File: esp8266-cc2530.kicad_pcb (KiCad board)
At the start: 2 copper layers, 119.9 x 53.1 mm, 35 parts, among them J1 CC2530_programmingHeader, J2 Conn_Coaxial, U1 WeMos_D1_mini, U2 AMS1117-3.3, U3 CC2530Fxxx, U4 RFX2401C, Y1 32.768kHz, Y2 32MHz

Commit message: progress on layout
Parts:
- removed C17: DNP, Capacitor_SMD:C_0805_2012Metric
- C1, C2, R1, U2: moved to B.Cu
- J1: footprint Connector_PinHeader_2.54mm:PinHeader_2x05_P2.54mm_Vertical_SMD -> Connector_PinHeader_1.27mm:PinHeader_2x05_P1.27mm_Vertical_SMD
- R5: moved to F.Cu
- moved C1 110.9 mm to (147.4, 136.8)
- moved C2 109.9 mm to (147.7, 139.6)
- moved U2 107.4 mm to (148.2, 145.1), turned to 0 degrees
- moved R1 97.3 mm to (139.7, 145.3), turned to 180 degrees
- moved C8 91.2 mm to (165.8, 125.2), turned to 270 degrees
- moved U1 90.0 mm to (118.1, 124.3)
- moved C3 89.4 mm to (151.1, 126.0)
- moved C12 88.7 mm to (158.8, 125.8), turned to 270 degrees
- moved R3 88.2 mm to (172.2, 128.4), turned to 90 degrees
- moved C10 87.6 mm to (157.3, 141.8)
- moved Y1 87.5 mm to (156.2, 138.8)
- moved C15 87.5 mm to (164.4, 129.8)
- moved C13 87.5 mm to (161.7, 132.6)
- moved C14 87.5 mm to (161.7, 130.7)
- moved C16 87.5 mm to (167.1, 132.7)
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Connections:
- R5 pad 1: Net-(J2-Pad1) -> VCC
- R5 pad 2: Net-(C17-Pad2) -> Net-(J1-Pad9)
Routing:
- net VCC: track 0.00 -> 66.7 mm, vias 0 -> 1
- net GND: track 0.00 -> 66.0 mm, vias 0 -> 18
- net /P2_1: track 0.00 -> 43.2 mm, vias 0 -> 1
- net /P1_1: track 0.00 -> 39.9 mm
- net /P2_2: track 0.00 -> 32.0 mm, vias 0 -> 1
- net /P1_0: track 0.00 -> 28.6 mm
- net /ESP_TX: track 0.00 -> 27.5 mm, vias 0 -> 1
- net /ESP_RX: track 0.00 -> 26.2 mm, vias 0 -> 1
- net Net-(R1-Pad2): track 0.00 -> 21.9 mm
- net Net-(J1-Pad9): track 0.00 -> 9.86 mm
- net Net-(C6-Pad2): track 0.00 -> 9.53 mm
- net Net-(C8-Pad2): track 0.00 -> 9.49 mm
- net Net-(C9-Pad2): track 0.00 -> 7.77 mm
- net Net-(R4-Pad1): track 0.00 -> 7.62 mm
- net Net-(C10-Pad2): track 0.00 -> 6.50 mm
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- added copper zone on F.Cu, net GND
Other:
- board size 119.9 x 53.1 mm -> 126.8 x 87.2 mm

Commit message: board laid out
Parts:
- moved L2 1.10 mm to (168.1, 130.8)
- moved C14 1.10 mm to (162.8, 130.7)
- moved C15 1.10 mm to (165.5, 129.8)
- moved C6 0.80 mm to (162.6, 123.2)
- moved C8 0.80 mm to (165.8, 126.0)
- moved Y2 0.80 mm to (162.7, 126.0)
- moved C5 0.38 mm to (151.6, 136.3)
- moved C4 0.20 mm to (150.6, 133.3)
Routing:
- net /~RST: track 0.00 -> 86.2 mm, vias 0 -> 3
- net VCC: track 66.7 -> 135.9 mm, vias 1 -> 9
- net /ESP_TX: track 27.5 -> 22.6 mm
- net /ESP_RX: track 26.2 -> 21.7 mm
- net /P1_0: track 28.6 -> 27.4 mm
- net Net-(C14-Pad1): track 2.42 -> 3.52 mm
- net Net-(C6-Pad2): track 9.53 -> 8.76 mm
- net GND: track 66.0 -> 66.5 mm, vias 18 -> 31
- net (no net): vias 0 -> 2
- added copper zone on B.Cu, net GND

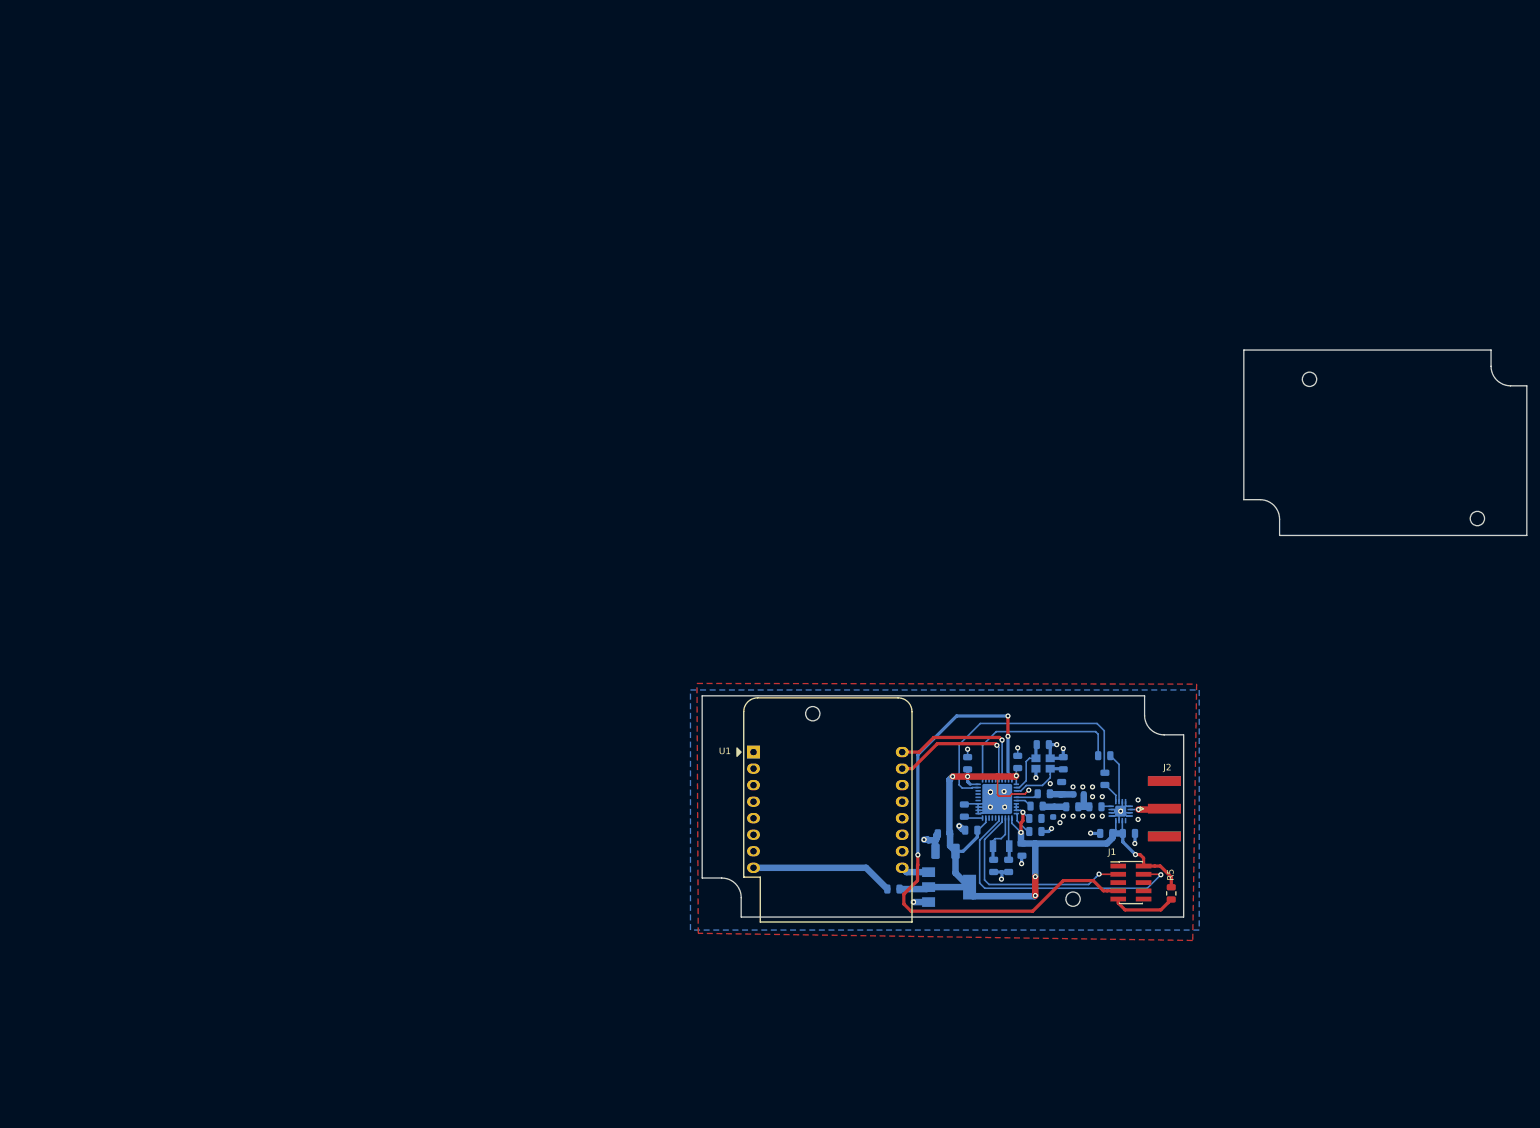
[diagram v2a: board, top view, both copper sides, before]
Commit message: fixed SMA connector footprint and added 3d model.
thinking of changing cases... extra board outlines on edge.cuts
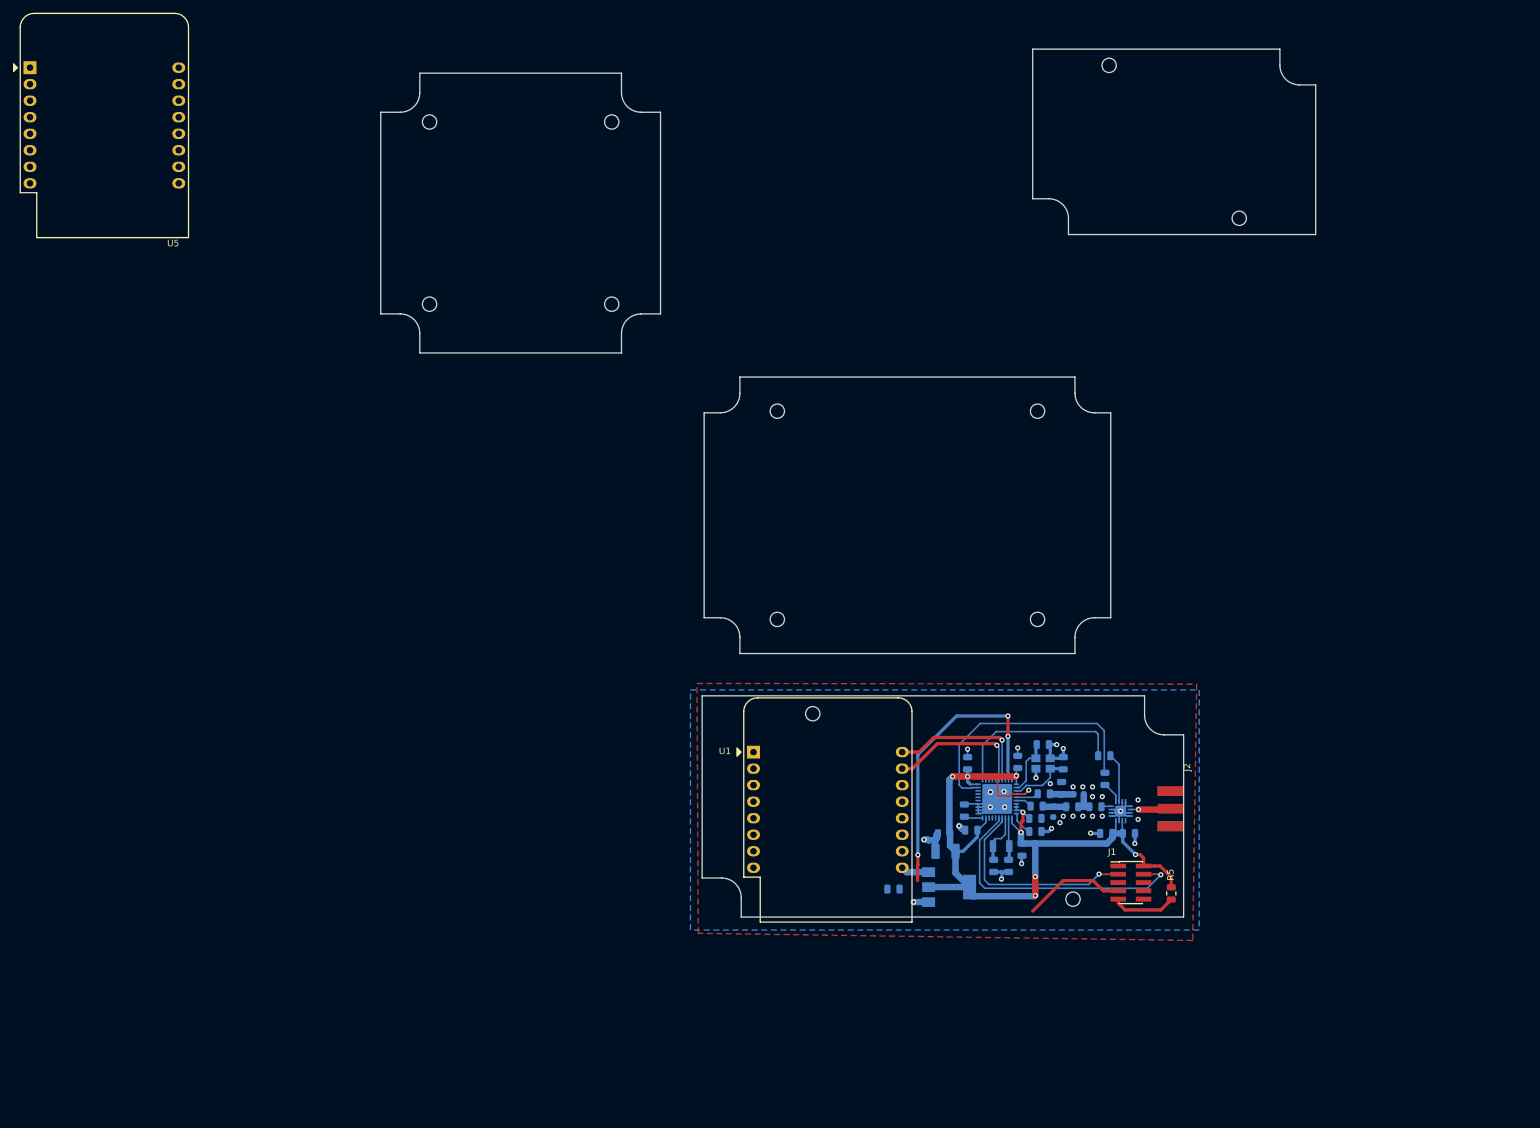
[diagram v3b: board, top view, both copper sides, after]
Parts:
- added U5: WeMos_D1_mini, Module:WEMOS_D1_mini_light, F.Cu at (6.94, 19.1)
- J2: footprint Connector_Coaxial:SMA_Amphenol_132289_EdgeMount -> esp8266-cc2530:CON-SMA-EDGE-S(RP)
- moved J2 0.95 mm to (182.2, 133.0), turned to 270 degrees
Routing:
- net /~RST: track 86.2 -> 61.5 mm
- net Net-(R1-Pad2): track 21.9 -> 0.00 mm
- net VCC: track 135.9 -> 131.7 mm
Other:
- board size 126.8 x 87.2 mm -> 143.7 x 133.4 mm

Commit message: updated layout * new WEMOS D1 footprint and 3d model * switched to case TW5-2-5
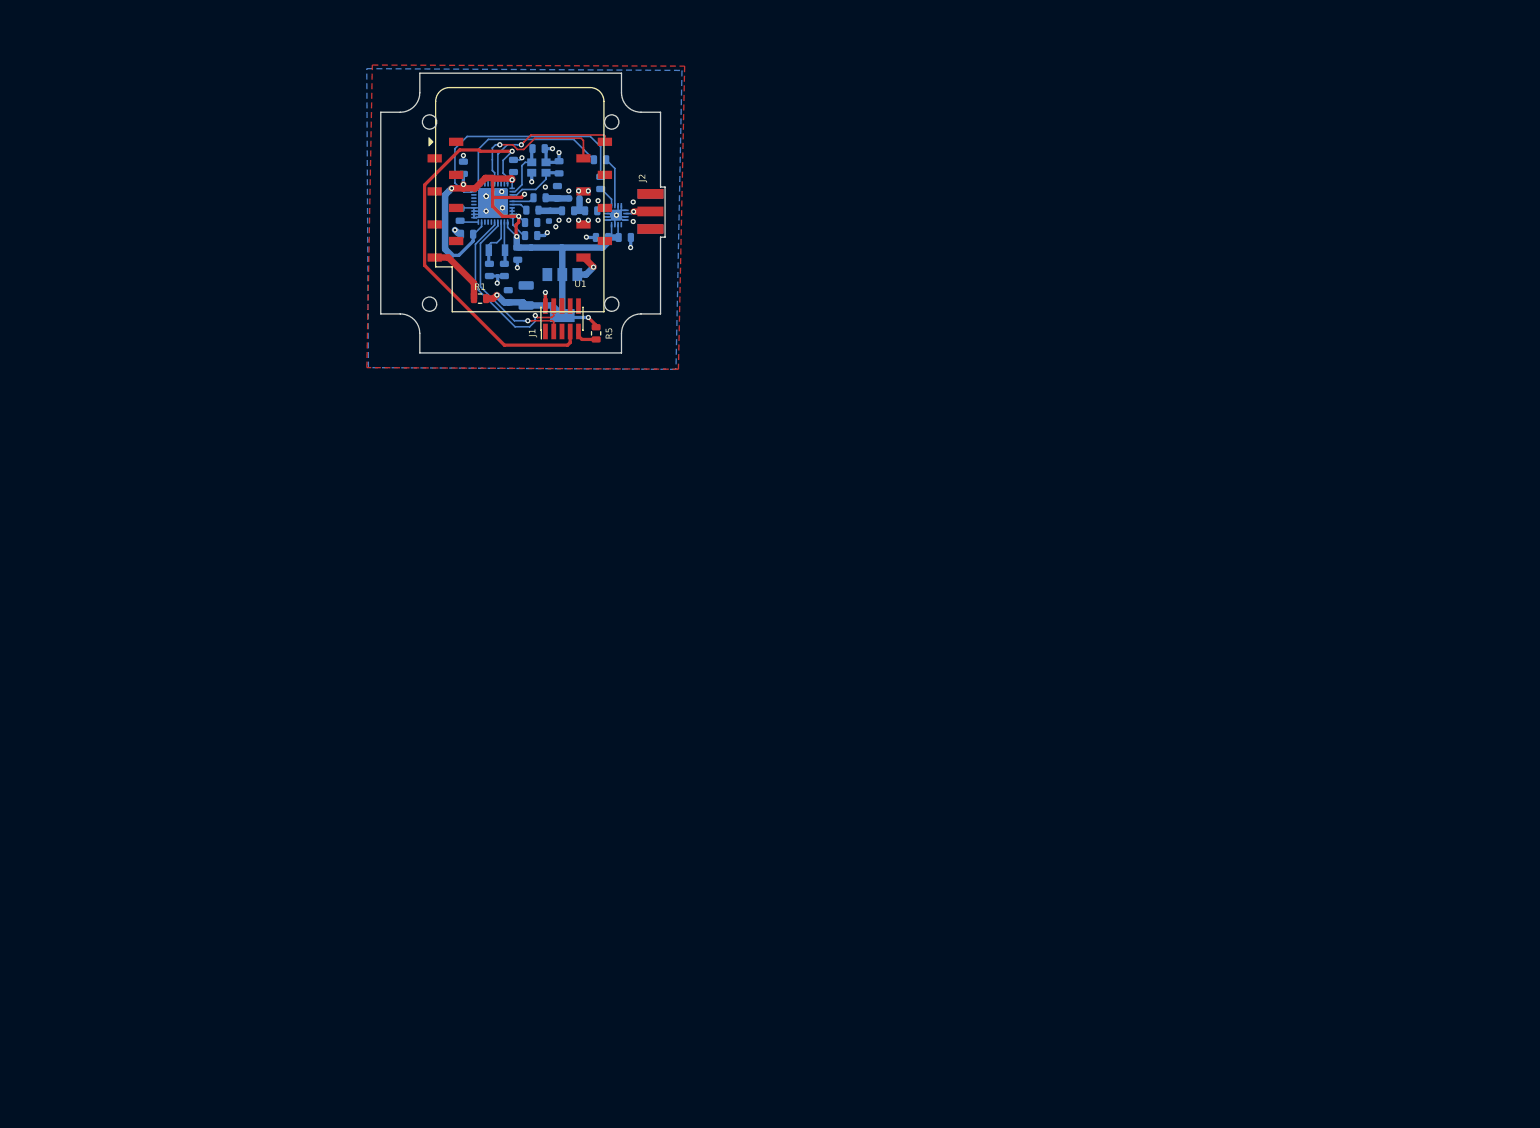
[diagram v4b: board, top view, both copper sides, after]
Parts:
- removed U5: WeMos_D1_mini, Module:WEMOS_D1_mini_light
- R1: moved to F.Cu
- U1: footprint Module:WEMOS_D1_mini_light -> esp8266-cc2530:WEMOS_D1_mini_smt
- moved R5 123.4 mm to (94.0, 59.9)
- moved J1 123.1 mm to (88.7, 57.7), turned to 90 degrees
- moved J2 121.7 mm to (102.3, 41.2)
- moved C15 120.0 mm to (88.0, 38.2)
- moved C19 120.0 mm to (94.9, 45.2)
- moved C5 120.0 mm to (74.1, 44.7)
- moved C6 120.0 mm to (85.1, 31.6)
- moved L2 120.0 mm to (90.6, 39.2)
- moved C10 120.0 mm to (79.8, 50.2)
- moved C11 120.0 mm to (84.0, 42.9)
- moved C12 120.0 mm to (81.2, 34.2)
- moved C13 120.0 mm to (84.2, 41.0)
- moved C14 120.0 mm to (85.3, 39.1)
- moved C16 120.0 mm to (89.6, 41.1)
- moved C18 120.0 mm to (93.2, 41.1)
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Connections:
- U1 pad 11: Net-(U1-Pad11) -> GND
- U1 pad 12: Net-(U1-Pad12) -> GND
- U1 pad 13: Net-(U1-Pad13) -> GND
- U1 pad 14: Net-(U1-Pad14) -> GND
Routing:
- net /P2_1: track 43.1 -> 28.7 mm
- net VCC: track 131.7 -> 119.8 mm
- net Net-(R1-Pad2): track 0.00 -> 10.0 mm
- net GND: track 66.5 -> 60.2 mm, vias 31 -> 29
- net Net-(J1-Pad9): track 9.86 -> 3.62 mm
- net /P2_2: track 32.1 -> 26.0 mm
- net /ESP_RX: track 21.7 -> 25.5 mm
- net /P1_1: track 40.0 -> 37.4 mm
- net /P1_0: track 27.4 -> 25.0 mm
- net /~RST: track 61.5 -> 63.3 mm, vias 3 -> 1
- net Net-(U1-Pad9): track 4.33 -> 5.14 mm, vias 0 -> 1
- net /ESP_TX: track 22.6 -> 23.2 mm
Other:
- board size 143.7 x 133.4 mm -> 43.7 x 43 mm

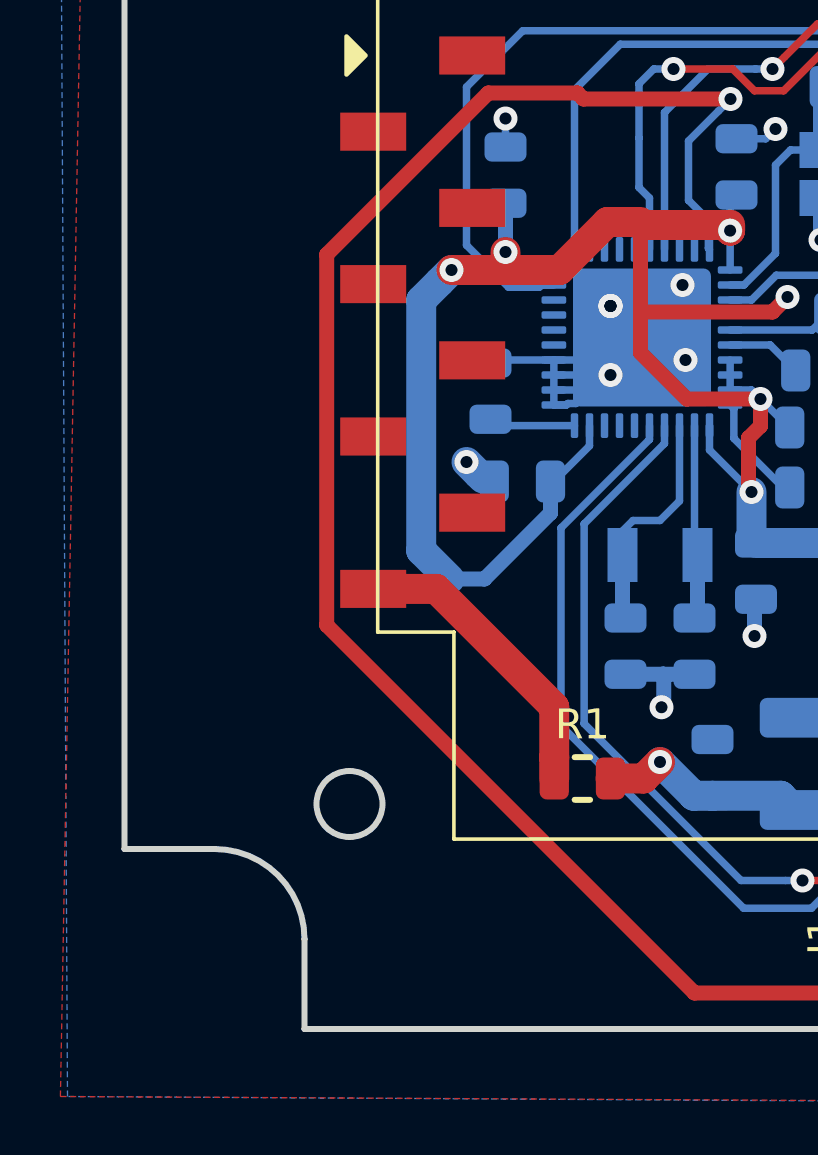
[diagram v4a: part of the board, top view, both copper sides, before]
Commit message: added usb connector, not routed yet
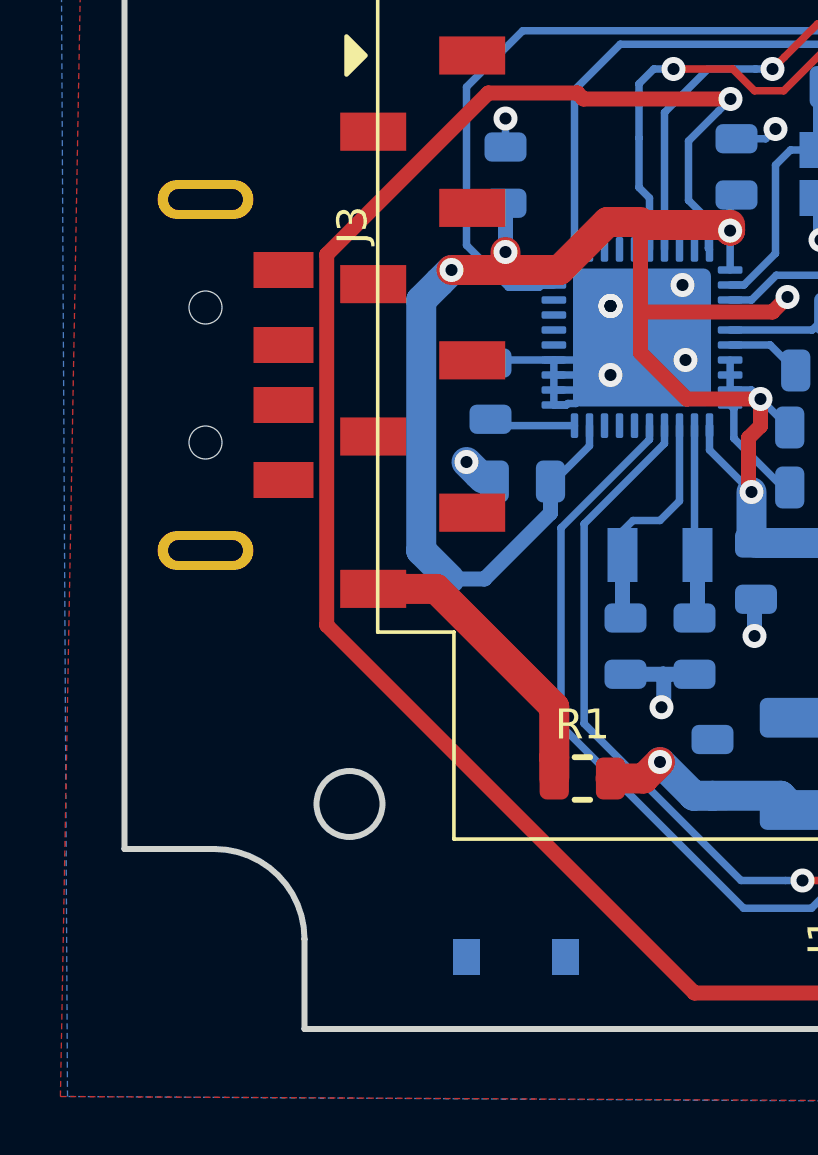
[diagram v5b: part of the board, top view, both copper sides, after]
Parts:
- added D1: B5819W, Diode_SMD:D_SOD-123, B.Cu at (73.9, 60.5)
- added J3: USB_A, esp8266-cc2530:Molex_48037-2200_USB-A, F.Cu at (63.5, 41.1)
